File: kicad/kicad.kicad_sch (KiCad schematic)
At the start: 249 parts, among them sw1 Esc, sw10 Z, sw100 N5, sw101 N6, sw102 N2, sw103 N1, sw104 N0, sw105 MPlay, sw106 MFwd, sw107 NSlash, sw108 NStar, sw109 N8, sw11 LCtrl, sw110 N9, sw111 NMinus, sw112 NPlus, sw113 NEnter, sw114 N3, sw115 NPeriod, sw12 LSys, sw13 F2, sw14 F3, sw15 2, sw16 3, sw17 W, sw18 E, sw19 S, sw2 F1, sw20 D, sw21 X, sw22 C, sw23 LAlt, sw24 THome, sw25 F4, sw26 F5, sw27 4, sw28 5, sw29 R, sw3 Tilda, sw30 T, sw31 F, sw32 G, sw33 V, sw34 B, sw35 LSpace, sw36 TLeft, sw37 F6, sw38 F7, sw39 6, sw4 1, sw40 7, sw41 Y, sw42 U, sw43 H, sw44 J, sw45 N, sw46 M, sw47 TUp, sw48 TDown, sw49 F8, sw5 Tab, sw50 F9, sw51 8, sw52 9, sw53 I, sw54 O, sw55 K, sw56 L, sw57 Comma, sw58 Period, sw59 RSpace, sw6 Q, sw60 TRight, sw61 F10, sw62 F11, sw63 0, sw64 Minus, sw65 P, sw66 LBrack, sw67 Semi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

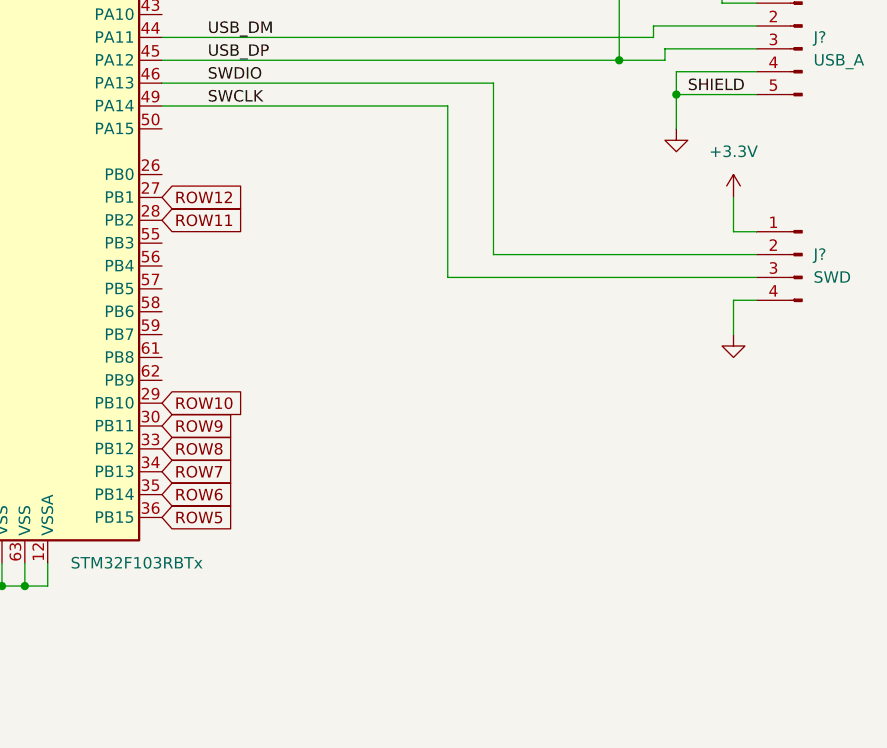
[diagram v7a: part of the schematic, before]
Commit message: Add caps lock led
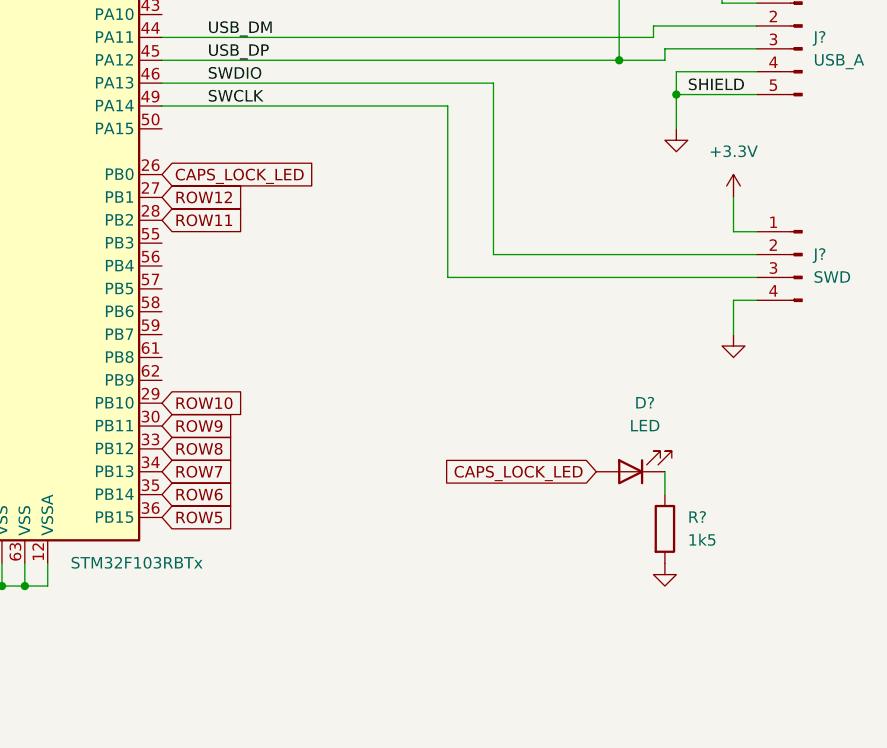
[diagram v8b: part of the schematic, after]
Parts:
- added D?: LED, symbol Device:LED
- added R?: 1k5, symbol Device:R
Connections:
- net GND: now also R?.2
- net CAPS_LOCK_LED: now reaches MCU1.26 (PB0)
- net CAPS_LOCK_LED: now also D?.2 (A)
- new net: D?.1 (K), R?.1
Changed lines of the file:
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@@
     (stroke (width 0) (type default) (color 0 0 0 0))
   )
+  (wire (pts (xy 436.88 151.13) (xy 436.88 153.67))
+    (stroke (width 0) (type default) (color 0 0 0 0))
+  )
   (wire (pts (xy 35.56 90.17) (xy 35.56 105.41))
     (stroke (width 0) (type default) (color 0 0 0 0))
@@
     )
   )
+  (global_label "CAPS_LOCK_LED" (shape input) (at 381 118.11 0) (fields_autoplaced)
+    (effects (font (size 1.27 1.27)) (justify left))
+    (property "Intersheet References" "${INTERSHEET_REFS}" (id 0) (at 398.5321 118.0306 0)
+      (effects (font (size 1.27 1.27)) (justify left) hide)
+    )
+  )
   (global_label "COLUMN8" (shape input) (at 381 80.01 0) (fields_autoplaced)
     (effects (font (size 1.27 1.27)) (justify left))
@@
     )
   )
+  (global_label "CAPS_LOCK_LED" (shape input) (at 429.26 151.13 180) (fields_autoplaced)
+    (effects (font (size 1.27 1.27)) (justify right))
+    (property "Intersheet References" "${INTERSHEET_REFS}" (id 0) (at 411.7279 151.0506 0)
+      (effects (font (size 1.27 1.27)) (justify right) hide)
+    )
+  )
   (global_label "ROW5" (shape input) (at 381 156.21 0) (fields_autoplaced)
     (effects (font (size 1.27 1.27)) (justify left))
@@
     (pin "2")
   )
+  (symbol (lib_id "power:GND") (at 436.88 161.29 0) (unit 1)
+    (in_bom yes) (on_board yes) (fields_autoplaced)
+    (property "Reference" "#PWR?" (id 0) (at 436.88 167.64 0)
+      (effects (font (size 1.27 1.27)) hide)
+    )
+    (property "Value" "GND" (id 1) (at 436.88 166.37 0)
+      (effects (font (size 1.27 1.27)) hide)
+    )
+    (property "Footprint" "" (id 2) (at 436.88 161.29 0)
+      (effects (font (size 1.27 1.27)) hide)
+    )
+    (property "Datasheet" "" (id 3) (at 436.88 161.29 0)
+      (effects (font (size 1.27 1.27)) hide)
+    )
+    (pin "1")
+  )
   (symbol (lib_id "Switch:SW_Push") (at 130.81 147.32 0) (unit 1)
     (in_bom yes) (on_board yes) (fields_autoplaced)
@@
     (pin "2")
   )
+  (symbol (lib_id "Device:LED") (at 433.07 151.13 180) (unit 1)
+    (in_bom yes) (on_board yes) (fields_autoplaced)
+    (property "Reference" "D?" (id 0) (at 434.6575 143.51 0))
+    (property "Value" "LED" (id 1) (at 434.6575 146.05 0))
+    (property "Footprint" "" (id 2) (at 433.07 151.13 0)
+      (effects (font (size 1.27 1.27)) hide)
+    )
+    (property "Datasheet" "~" (id 3) (at 433.07 151.13 0)
+      (effects (font (size 1.27 1.27)) hide)
+    )
+    (pin "1")
+    (pin "2")
+  )
   (symbol (lib_id "pspice:DIODE") (at 41.91 135.89 180) (unit 1)
     (in_bom yes) (on_board yes) (fields_autoplaced)
@@
     (pin "2")
   )
+  (symbol (lib_id "Device:R") (at 436.88 157.48 0) (unit 1)
+    (in_bom yes) (on_board yes) (fields_autoplaced)
+    (property "Reference" "R?" (id 0) (at 439.42 156.2099 0)
+      (effects (font (size 1.27 1.27)) (justify left))
+    )
+    (property "Value" "1k5" (id 1) (at 439.42 158.7499 0)
+      (effects (font (size 1.27 1.27)) (justify left))
+    )
+    (property "Footprint" "" (id 2) (at 435.102 157.48 90)
+      (effects (font (size 1.27 1.27)) hide)
+    )
+    (property "Datasheet" "~" (id 3) (at 436.88 157.48 0)
+      (effects (font (size 1.27 1.27)) hide)
+    )
+    (pin "1")
+    (pin "2")
+  )
   (symbol (lib_id "pspice:DIODE") (at 92.71 135.89 180) (unit 1)
     (in_bom yes) (on_board yes) (fields_autoplaced)
@@
       (reference "#PWR?") (unit 1) (value "+3.3VA") (footprint "")
     )
+    (path "/6173d2b9-6720-4d65-a983-a45a9039f1ab"
+      (reference "#PWR?") (unit 1) (value "GND") (footprint "")
+    )
     (path "/653534d5-ec8c-4542-a47c-dbc9a7c01f08"
       (reference "#PWR?") (unit 1) (value "+3.3V") (footprint "")
@@
       (reference "D?") (unit 1) (value "LED") (footprint "")
     )
+    (path "/ca740f73-2198-47e1-bd9e-360e8c7fc27d"
+      (reference "D?") (unit 1) (value "LED") (footprint "")
+    )
     (path "/03cc42cf-3077-4072-8d68-4d42e27bd45c"
       (reference "J?") (unit 1) (value "USB_A") (footprint "")
@@
       (reference "R?") (unit 1) (value "1k5") (footprint "")
     )
+    (path "/e1999cf3-52b8-494c-8087-dbfd77e26283"
+      (reference "R?") (unit 1) (value "1k5") (footprint "")
+    )
